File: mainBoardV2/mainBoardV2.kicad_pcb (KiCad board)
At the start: 2 copper layers, 41.7 x 49.6 mm, 24 parts, among them J1 USB4125-GF-A_REVA2, U3 MCP73871-2AAI_ML, U4 MPU6050_Module, U5 TPS61023DRLT

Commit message: 3.12.26.C1
Seems this board is close to done. Need to discuss where our pushbutton and on/of switch would connect.
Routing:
- net /VoutBoost: track 25.8 -> 47.2 mm, vias 0 -> 2
- net /VBatt+: track 25.7 -> 28.4 mm
- net /VPCC: track 9.04 -> 11.1 mm
- net GND: track 24.6 -> 23.9 mm, vias 40 -> 51
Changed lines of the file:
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@@
-	)
-	(segment
-		(start 123.9475 116.324)
-		(end 124.418 115.8535)
-		(width 0.2)
-		(layer "F.Cu")
-		(net 4)
 	)
 	(segment
@@
 	)
 	(via
+		(at 106.4 121.2)
+		(size 0.6)
+		(drill 0.3)
+		(layers "F.Cu" "B.Cu")
+		(free yes)
+		(net 4)
+	)
+	(via
+		(at 105.7 121.2)
+		(size 0.6)
+		(drill 0.3)
+		(layers "F.Cu" "B.Cu")
+		(free yes)
+		(net 4)
+	)
+	(via
 		(at 102.2 119.7875)
 		(size 0.6)
@@
 	)
 	(via
+		(at 105 121.2)
+		(size 0.6)
+		(drill 0.3)
+		(layers "F.Cu" "B.Cu")
+		(free yes)
+		(net 4)
+	)
+	(via
 		(at 125.35 113.55)
 		(size 0.6)
@@
 	)
 	(via
+		(at 103.6 121.2)
+		(size 0.6)
+		(drill 0.3)
+		(layers "F.Cu" "B.Cu")
+		(free yes)
+		(net 4)
+	)
+	(via
 		(at 95.15 114.4)
 		(size 0.6)
@@
 	)
 	(via
+		(at 104.3 121.2)
+		(size 0.6)
+		(drill 0.3)
+		(layers "F.Cu" "B.Cu")
+		(free yes)
+		(net 4)
+	)
+	(via
+		(at 103.6 121.9)
+		(size 0.6)
+		(drill 0.3)
+		(layers "F.Cu" "B.Cu")
+		(free yes)
+		(net 4)
+	)
+	(via
 		(at 104.3 120.4875)
 		(size 0.6)
@@
 	)
 	(via
+		(at 105.7 121.9)
+		(size 0.6)
+		(drill 0.3)
+		(layers "F.Cu" "B.Cu")
+		(free yes)
+		(net 4)
+	)
+	(via
+		(at 105 121.9)
+		(size 0.6)
+		(drill 0.3)
+		(layers "F.Cu" "B.Cu")
+		(free yes)
+		(net 4)
+	)
+	(via
 		(at 113.25 122.75)
 		(size 0.6)
@@
 	)
 	(via
+		(at 102.9 121.2)
+		(size 0.6)
+		(drill 0.3)
+		(layers "F.Cu" "B.Cu")
+		(free yes)
+		(net 4)
+	)
+	(via
 		(at 125.25 116.8)
 		(size 0.6)
@@
 	)
 	(via
+		(at 104.3 121.9)
+		(size 0.6)
+		(drill 0.3)
+		(layers "F.Cu" "B.Cu")
+		(free yes)
+		(net 4)
+	)
+	(via
 		(at 118.1 114.8)
 		(size 0.6)
@@
 	(via
 		(at 114.95 118.9)
+		(size 0.6)
+		(drill 0.3)
+		(layers "F.Cu" "B.Cu")
+		(free yes)
+		(net 4)
+	)
+	(via
+		(at 106.4 121.9)
 		(size 0.6)
 		(drill 0.3)
@@
 	)
 	(segment
+		(start 123.4 115)
+		(end 122.1 115)
+		(width 0.2)
+		(layer "F.Cu")
+		(net 10)
+	)
+	(segment
+		(start 122.1 115)
+		(end 121.8 115.3)
+		(width 0.2)
+		(layer "F.Cu")
+		(net 10)
+	)
+	(segment
 		(start 120.35 120.7)
-		(end 122.4 118.65)
+		(end 122.25 118.8)
 		(width 0.4)
 		(layer "F.Cu")
@@
 	)
 	(segment
-		(start 120.035 115.3)
-		(end 122.1 115.3)
+		(start 121.8 115.3)
+		(end 120.035 115.3)
 		(width 0.2)
 		(layer "F.Cu")
@@
 	)
 	(segment
-		(start 122.1 115.3)
-		(end 122.4 115)
-		(width 0.2)
+		(start 122.25 118.8)
+		(end 123.3 118.8)
+		(width 0.4)
 		(layer "F.Cu")
 		(net 10)
 	)
 	(via
-		(at 122.4 118.65)
+		(at 123.3 118.8)
 		(size 0.5)
 		(drill 0.3)
@@
 	)
 	(via
-		(at 122.4 115)
+		(at 123.4 115)
 		(size 0.5)
 		(drill 0.3)
@@
 	)
 	(segment
-		(start 122.4 118.65)
-		(end 122.4 115)
+		(start 123.3 115.9)
+		(end 123.3 118.8)
+		(width 0.4)
+		(layer "B.Cu")
+		(net 10)
+	)
+	(segment
+		(start 123.4 115.8)
+		(end 123.3 115.9)
+		(width 0.4)
+		(layer "B.Cu")
+		(net 10)
+	)
+	(segment
+		(start 123.4 115)
+		(end 123.4 115.8)
 		(width 0.4)
 		(layer "B.Cu")
@@
 	)
 	(segment
-		(start 106.8875 123.4)
+		(start 100.8 128.2)
+		(end 103.2 128.2)
+		(width 0.8)
+		(layer "F.Cu")
+		(net 16)
+	)
+	(segment
+		(start 99.6 127)
+		(end 100.8 128.2)
+		(width 0.8)
+		(layer "F.Cu")
+		(net 16)
+	)
+	(segment
+		(start 114.3875 117.0125)
 		(end 114.3875 115.9)
-		(width 0.8)
-		(layer "F.Cu")
-		(net 16)
-	)
-	(segment
-		(start 99.6 125.8)
-		(end 99.6 124.7)
 		(width 0.8)
 		(layer "F.Cu")
@@
 	)
 	(segment
-		(start 99.6 124.7)
-		(end 100.9 123.4)
+		(start 99.6 125.8)
+		(end 99.6 127)
 		(width 0.8)
 		(layer "F.Cu")
@@
 	)
 	(segment
-		(start 100.9 123.4)
-		(end 106.8875 123.4)
+		(start 103.2 128.2)
+		(end 114.3875 117.0125)
 		(width 0.8)
 		(layer "F.Cu")
@@
 	)
 	(segment
-		(start 121.8565 115.8)
-		(end 121.8725 115.816)
-		(width 0.2)
+		(start 121.8625 116.4)
+		(end 121.8625 118.040996)
+		(width 0.8)
+		(layer "F.Cu")
+		(net 17)
+	)
+	(segment
+		(start 121.8625 118.040996)
+		(end 120.903496 119)
+		(width 0.8)
 		(layer "F.Cu")
 		(net 17)
@@
 	)
 	(segment
+		(start 120.903496 119)
+		(end 120.2 119)
+		(width 0.8)
+		(layer "F.Cu")
+		(net 17)
+	)
+	(segment
 		(start 100.5 89.78)
 		(end 98.49 87.77)
 		(width 0.8)
 		(layer "F.Cu")
+		(net 17)
+	)
+	(via
+		(at 120.2 119)
+		(size 0.6)
+		(drill 0.3)
+		(layers "F.Cu" "B.Cu")
+		(net 17)
+	)
+	(via
+		(at 104.3 116.25)
+		(size 0.6)
+		(drill 0.3)
+		(layers "F.Cu" "B.Cu")
+		(net 17)
+	)
+	(segment
+		(start 104.35 116.3)
+		(end 104.3 116.25)
+		(width 0.8)
+		(layer "B.Cu")
+		(net 17)
+	)
+	(segment
+		(start 110.201 119.801)
+		(end 106.7 116.3)
+		(width 0.8)
+		(layer "B.Cu")
+		(net 17)
+	)
+	(segment
+		(start 120.2 119)
+		(end 119.399 119.801)
+		(width 0.8)
+		(layer "B.Cu")
+		(net 17)
+	)
+	(segment
+		(start 119.399 119.801)
+		(end 110.201 119.801)
+		(width 0.8)
+		(layer "B.Cu")
+		(net 17)
+	)
+	(segment
+		(start 106.7 116.3)
+		(end 104.35 116.3)
+		(width 0.8)
+		(layer "B.Cu")
 		(net 17)
 	)
@@
 		(polygon
 			(pts
-				(xy 106.85 117.6875) (xy 106.85 122.6875) (xy 103.3 122.6875) (xy 100 117.9875) (xy 99.6 117.9875)
+				(xy 106.85 117.6875) (xy 106.85 122.3875) (xy 103.3 122.3875) (xy 100 117.9875) (xy 99.6 117.9875)
 				(xy 99.6 117.6875)
 			)
@@
 			(pts
 				(xy 97.5 122.6875) (xy 97.5 118.1875) (xy 98.9 118.1875) (xy 98.9 117.1875) (xy 97.1 117.1875) (xy 97.1 116.0875)
-				(xy 95.6 116.0875) (xy 95.6 118.54375) (xy 92.3 118.59375) (xy 92.3 122.6875)
+				(xy 95.6 116.0875) (xy 95.6 118.54375) (xy 95.6 118.59375) (xy 95.6 122.6875)
 			)
 		)

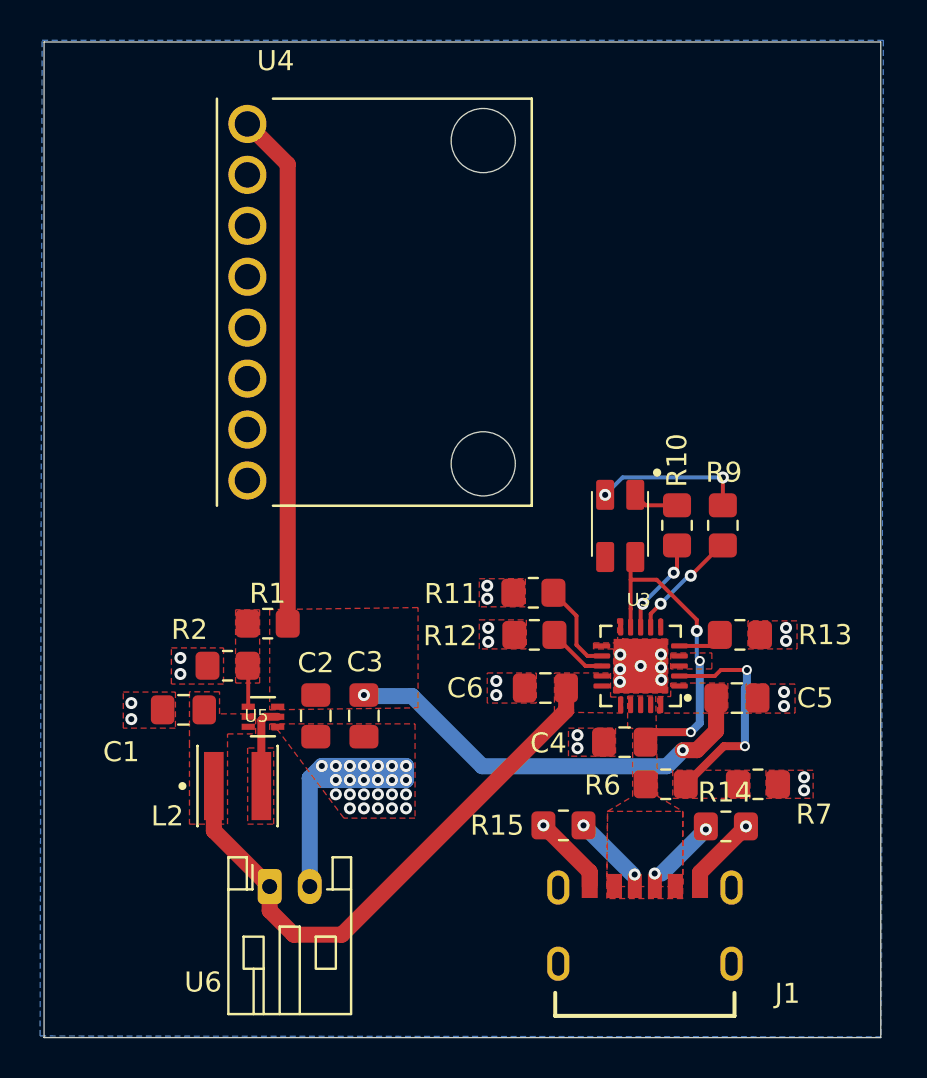
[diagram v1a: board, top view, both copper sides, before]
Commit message: 3.16.23.C1
Rotated IMU for a more compact design, per Connor's suggestion
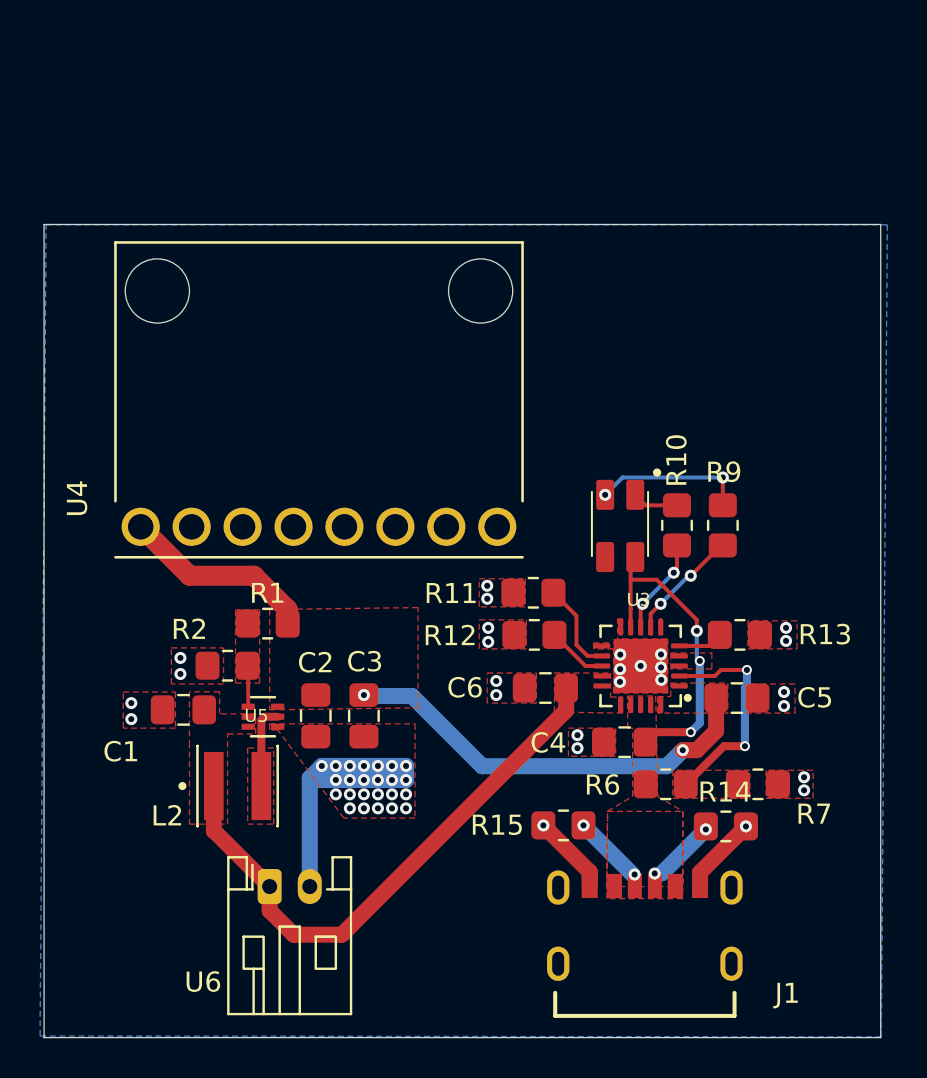
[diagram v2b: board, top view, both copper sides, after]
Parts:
- moved U4 5.60 mm to (102.1, 101.5), turned to 90 degrees
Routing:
- net /VoutBoost: track 47.2 -> 31.1 mm
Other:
- board size 41.7 x 49.6 mm -> 41.7 x 40.5 mm
- board text removed: "ON/OFF here"
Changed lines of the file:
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@@
 	(footprint "OC09600:MODULE_OC09600"
 		(layer "F.Cu")
-		(at 104.82 96.66)
+		(at 102.06 101.53 90)
 		(property "Reference" "U4"
-			(at -4.925 -12.035 0)
+			(at -4.925 -12.035 90)
 			(layer "F.SilkS")
 			(effects
@@
 		)
 		(property "Value" "MPU6050_Module"
-			(at 0.79 12.035 0)
+			(at 0.79 12.035 90)
 			(layer "F.Fab")
 			(effects
@@
 		)
 		(property "Datasheet" ""
-			(at 0 0 0)
+			(at 0 0 90)
 			(layer "F.Fab")
 			(hide yes)
@@
 		)
 		(property "Description" ""
-			(at 0 0 0)
+			(at 0 0 90)
 			(layer "F.Fab")
 			(hide yes)
@@
 		)
 		(property "MF" "YKS"
-			(at 0 0 0)
+			(at 0 0 90)
 			(unlocked yes)
 			(layer "F.Fab")
@@
 		)
 		(property "MAXIMUM_PACKAGE_HEIGHT" "3.00mm"
-			(at 0 0 0)
+			(at 0 0 90)
 			(unlocked yes)
 			(layer "F.Fab")
@@
 		)
 		(property "CREATOR" "ANA"
-			(at 0 0 0)
+			(at 0 0 90)
 			(unlocked yes)
 			(layer "F.Fab")
@@
 		)
 		(property "Price" "None"
-			(at 0 0 0)
+			(at 0 0 90)
 			(unlocked yes)
 			(layer "F.Fab")
@@
 		)
 		(property "Package" "None"
-			(at 0 0 0)
+			(at 0 0 90)
 			(unlocked yes)
 			(layer "F.Fab")
@@
 		)
 		(property "Check_prices" "https://www.snapeda.com/parts/OC09600/YKS/view-part/?ref=eda"
-			(at 0 0 0)
+			(at 0 0 90)
 			(unlocked yes)
 			(layer "F.Fab")
@@
 		)
 		(property "STANDARD" "Manufacturer Recommendations"
-			(at 0 0 0)
+			(at 0 0 90)
 			(unlocked yes)
 			(layer "F.Fab")
@@
 		)
 		(property "PARTREV" "NA"
-			(at 0 0 0)
+			(at 0 0 90)
 			(unlocked yes)
 			(layer "F.Fab")
@@
 		)
 		(property "VERIFIER" ""
-			(at 0 0 0)
+			(at 0 0 90)
 			(unlocked yes)
 			(layer "F.Fab")
@@
 		)
 		(property "SnapEDA_Link" "https://www.snapeda.com/parts/OC09600/YKS/view-part/?ref=snap"
-			(at 0 0 0)
+			(at 0 0 90)
 			(unlocked yes)
 			(layer "F.Fab")
@@
 		)
 		(property "MP" "OC09600"
-			(at 0 0 0)
+			(at 0 0 90)
 			(unlocked yes)
 			(layer "F.Fab")
@@
 		)
 		(property "Description_1" "GY-521 6 DOF MPU-6050 Module 3 Axis Accelerometer Gyroscope Module for Arduino"
-			(at 0 0 0)
+			(at 0 0 90)
 			(unlocked yes)
 			(layer "F.Fab")
@@
 		)
 		(property "Availability" "Not in stock"
-			(at 0 0 0)
+			(at 0 0 90)
 			(unlocked yes)
 			(layer "F.Fab")
@@
 		)
 		(property "MANUFACTURER" "YKS"
-			(at 0 0 0)
+			(at 0 0 90)
 			(unlocked yes)
 			(layer "F.Fab")
@@
 		(attr through_hole)
 		(fp_line
-			(start -7.85 10.15)
-			(end -7.85 -10.15)
+			(start 7.85 -10.15)
+			(end 7.85 10.15)
 			(stroke
 				(width 0.127)
@@
 		)
 		(fp_line
-			(start 7.85 -10.15)
-			(end 7.85 10.15)
+			(start 7.85 10.15)
+			(end -5.0575 10.15)
 			(stroke
 				(width 0.127)
@@
 		)
 		(fp_line
-			(start 7.85 10.15)
-			(end -5.0575 10.15)
+			(start -7.85 10.15)
+			(end -7.85 -10.15)
 			(stroke
 				(width 0.127)
@@
 		)
 		(fp_line
-			(start -8.1 -10.4)
-			(end -8.1 10.4)
+			(start 8.1 -10.4)
+			(end -8.1 -10.4)
 			(stroke
 				(width 0.05)
@@
 		)
 		(fp_line
-			(start -8.1 10.4)
-			(end 8.1 10.4)
+			(start -8.1 -10.4)
+			(end -8.1 10.4)
 			(stroke
 				(width 0.05)
@@
 		)
 		(fp_line
-			(start 8.1 -10.4)
-			(end -8.1 -10.4)
+			(start 8.1 10.4)
+			(end 8.1 -10.4)
 			(stroke
 				(width 0.05)
@@
 		)
 		(fp_line
-			(start 8.1 10.4)
-			(end 8.1 -10.4)
+			(start -8.1 10.4)
+			(end 8.1 10.4)
 			(stroke
 				(width 0.05)
@@
 		)
 		(fp_line
-			(start -7.85 -10.15)
-			(end 7.85 -10.15)
+			(start 7.85 -10.15)
+			(end 7.85 10.15)
 			(stroke
 				(width 0.127)
@@
 		)
 		(fp_line
-			(start -7.85 10.15)
-			(end -7.85 -10.15)
+			(start -7.85 -10.15)
+			(end 7.85 -10.15)
 			(stroke
 				(width 0.127)
@@
 		)
 		(fp_line
-			(start 7.85 -10.15)
-			(end 7.85 10.15)
+			(start 7.85 10.15)
+			(end -7.85 10.15)
 			(stroke
 				(width 0.127)
@@
 		)
 		(fp_line
-			(start 7.85 10.15)
-			(end -7.85 10.15)
+			(start -7.85 10.15)
+			(end -7.85 -10.15)
 			(stroke
 				(width 0.127)
@@
 		)
 		(pad "" np_thru_hole circle
-			(at 5.43 -8.06)
+			(at 5.43 -8.06 90)
 			(size 3.2 3.2)
 			(drill 3.2)
@@
 		)
 		(pad "" np_thru_hole circle
-			(at 5.43 8.06)
+			(at 5.43 8.06 90)
 			(size 3.2 3.2)
 			(drill 3.2)
@@
 		)
 		(pad "AD0" thru_hole circle
-			(at -6.33 6.35)
+			(at -6.33 6.35 90)
 			(size 1.905 1.905)
 			(drill 1.27)
@@
 		)
 		(pad "GND" thru_hole circle
-			(at -6.33 -6.35)
+			(at -6.33 -6.35 90)
 			(size 1.905 1.905)
 			(drill 1.27)
@@
 		)
 		(pad "INT" thru_hole circle
-			(at -6.33 8.89)
+			(at -6.33 8.89 90)
 			(size 1.905 1.905)
 			(drill 1.27)
@@
 		)
 		(pad "SCL" thru_hole circle
-			(at -6.33 -3.81)
+			(at -6.33 -3.81 90)
 			(size 1.905 1.905)
 			(drill 1.27)
@@
 		)
 		(pad "SDA" thru_hole circle
-			(at -6.33 -1.27)
+			(at -6.33 -1.27 90)
 			(size 1.905 1.905)
 			(drill 1.27)
@@
 		)
 		(pad "VCC" thru_hole circle
-			(at -6.33 -8.89)
+			(at -6.33 -8.89 90)
 			(size 1.905 1.905)
 			(drill 1.27)
@@
 		)
 		(pad "XCL" thru_hole circle
-			(at -6.33 3.81)
+			(at -6.33 3.81 90)
 			(size 1.905 1.905)
 			(drill 1.27)
@@
 		)
 		(pad "XDA" thru_hole circle
-			(at -6.33 1.27)
+			(at -6.33 1.27 90)
 			(size 1.905 1.905)
 			(drill 1.27)
@@
 	)
 	(gr_rect
-		(start 88.35 83.684)
+		(start 88.35 92.784)
 		(end 130.072 133.332)
 		(stroke
@@
 		(layer "Edge.Cuts")
 	)
-	(gr_text "ON/OFF here"
-		(at 89.7 109.2 0)
-		(layer "Cmts.User")
-		(effects
-			(font
-				(size 1 1)
-				(thickness 0.15)
-			)
-			(justify left bottom)
-		)
-	)
 	(segment
 		(start 118.809958 125.17)
@@
 	)
 	(segment
-		(start 100.5 112.6875)
-		(end 100.5 89.78)
+		(start 120.903496 119)
+		(end 120.2 119)
 		(width 0.8)
 		(layer "F.Cu")
@@
 	)
 	(segment
-		(start 120.903496 119)
-		(end 120.2 119)
-		(width 0.8)
+		(start 100.5 112.6875)
+		(end 100.5 111.9875)
+		(width 1)
 		(layer "F.Cu")
 		(net 17)
 	)
 	(segment
-		(start 100.5 89.78)
-		(end 98.49 87.77)
-		(width 0.8)
+		(start 95.61 110.3)
+		(end 93.17 107.86)
+		(width 1)
+		(layer "F.Cu")
+		(net 17)
+	)
+	(segment
+		(start 98.8125 110.3)
+		(end 95.61 110.3)
+		(width 1)
+		(layer "F.Cu")
+		(net 17)
+	)
+	(segment
+		(start 100.5 111.9875)
+		(end 98.8125 110.3)
+		(width 1)
 		(layer "F.Cu")
 		(net 17)
@@
 		(polygon
 			(pts
-				(xy 88.252577 83.6) (xy 130.202577 83.6) (xy 130.102577 133.3) (xy 88.152577 133.25)
+				(xy 88.452577 92.8) (xy 130.402577 92.8) (xy 130.102577 133.3) (xy 88.152577 133.25)
 			)
 		)

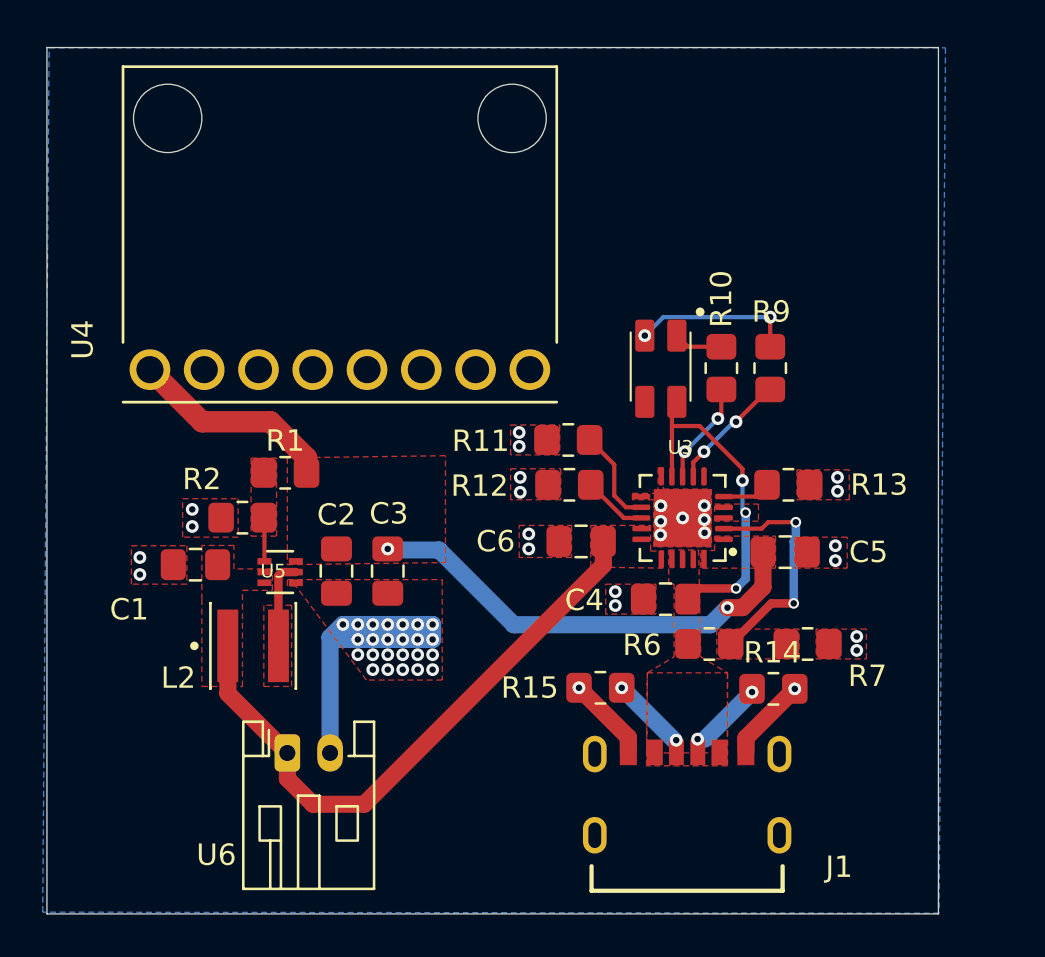
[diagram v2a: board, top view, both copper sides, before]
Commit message: 3.17.26.C1
inserted a true NTC thermistor, set to operate from 0 to 50C. Added two Vout vias for use with the board outside of the connection to the IMU. Add through holes to feed jst wires or the NTC bead through. Added notes to schematic, and included ESP32 devkit, 2 cams on the schematic (but not board)
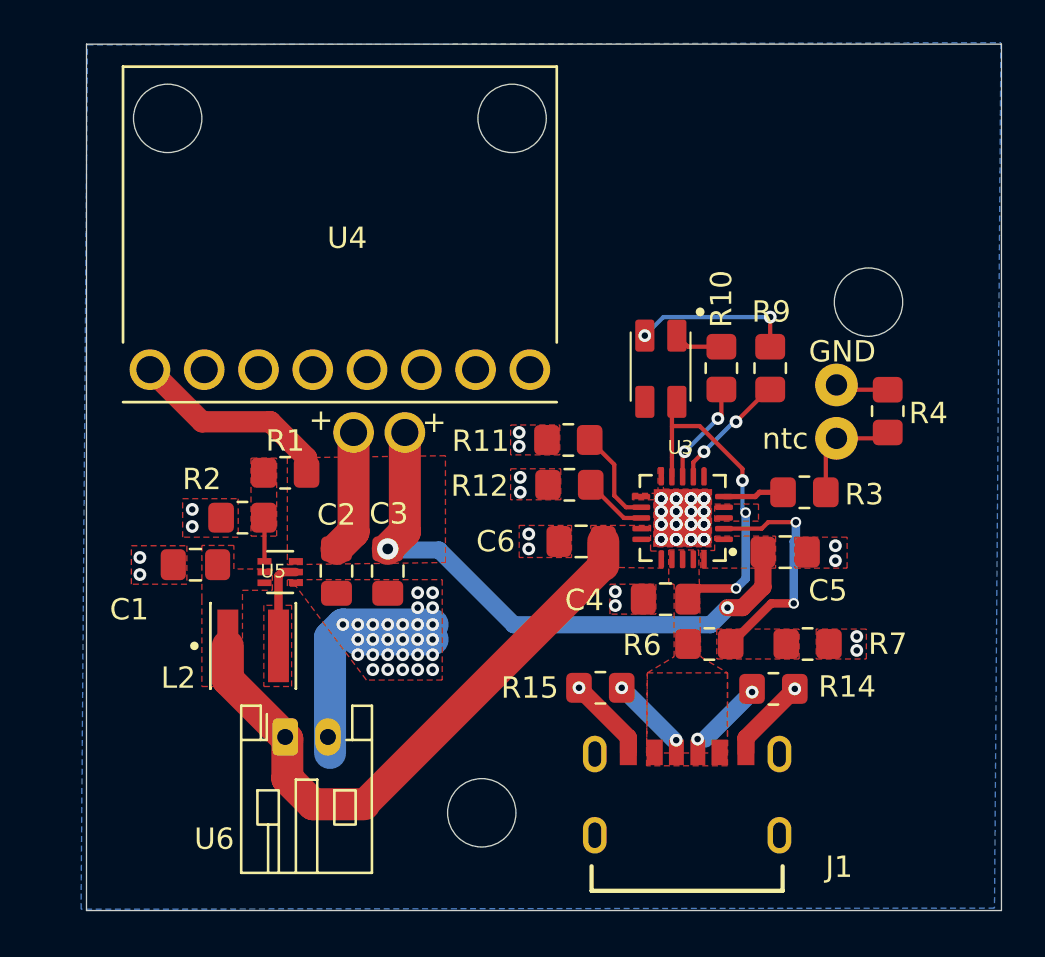
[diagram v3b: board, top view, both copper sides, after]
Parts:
- added ?: , , F.Cu at (105.1, 110.8)
- added ?: , , F.Cu at (126.8, 104.7)
- added ?: , , F.Cu at (108.7, 128.6)
- added ?: , , F.Cu at (102.7, 110.8)
- added R3: 1.5k, Resistor_SMD:R_0805_2012Metric_Pad1.20x1.40mm_HandSolder, F.Cu at (123.8, 113.6)
- added R4: 70k, Resistor_SMD:R_0805_2012Metric_Pad1.20x1.40mm_HandSolder, F.Cu at (127.7, 109.8)
- ntc: renamed from R13; footprint Resistor_SMD:R_0805_2012Metric_Pad1.20x1.40mm_HandSolder -> TPS61023DRLT:103AT-11_NTC_throughole
- moved ntc 2.27 mm to (125.3, 113.6), turned to 0 degrees
- moved U6 0.76 mm to (99.5, 125.0)
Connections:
- J1 pad S1: unconnected-(J1-SHIELD-PadS1)_3 -> GND
- J1 pad S2: unconnected-(J1-SHIELD-PadS1) -> GND
- J1 pad S3: unconnected-(J1-SHIELD-PadS1)_2 -> GND
- J1 pad S4: unconnected-(J1-SHIELD-PadS1)_1 -> GND
- ntc pad 2: /Therm -> Net-(R13-Pad2)
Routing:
- net /VoutBoost: track 31.1 -> 42.7 mm
- net Net-(R13-Pad2): track 0.00 -> 5.25 mm
- net GND: track 23.9 -> 26.4 mm, vias 51 -> 78
- net /Therm: track 2.24 -> 2.85 mm
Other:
- board size 41.7 x 40.5 mm -> 42.8 x 40.5 mm
- board text added: "+"
- board text added: "GND"
